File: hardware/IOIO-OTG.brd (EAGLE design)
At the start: 68.6 x 30.5 mm, 60 parts, among them Q1 IRLML2244, Q2 2N7002PW, Q3 MOSFET-NCHANNELAO3404A, U1 PIC24FJ256GB206, U2 TPS62133RGTT, U3 MIC5216

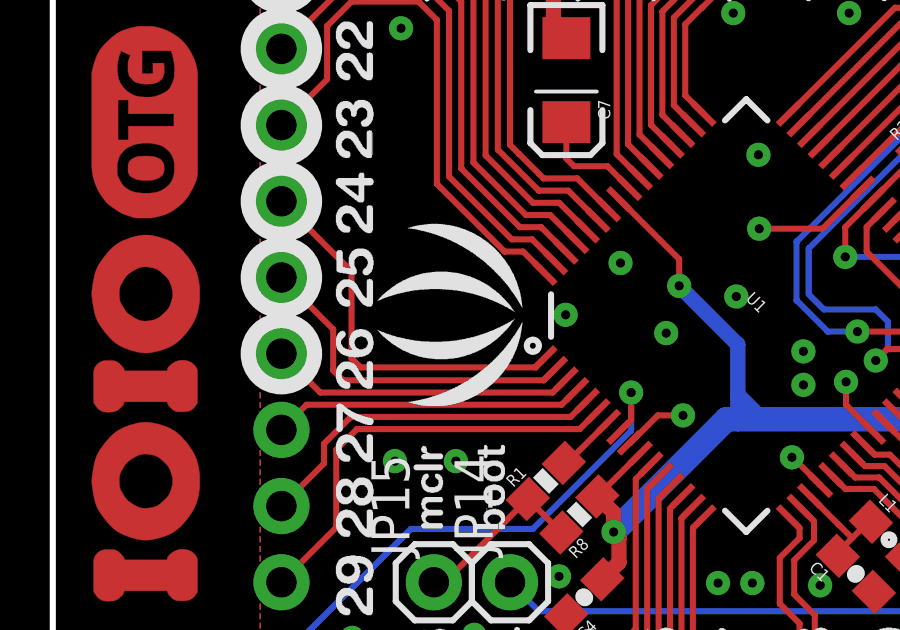
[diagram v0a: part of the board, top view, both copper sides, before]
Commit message: SparkFun Logo
Also, changed to v22a in schematic (it was still v22b from the copy
over)
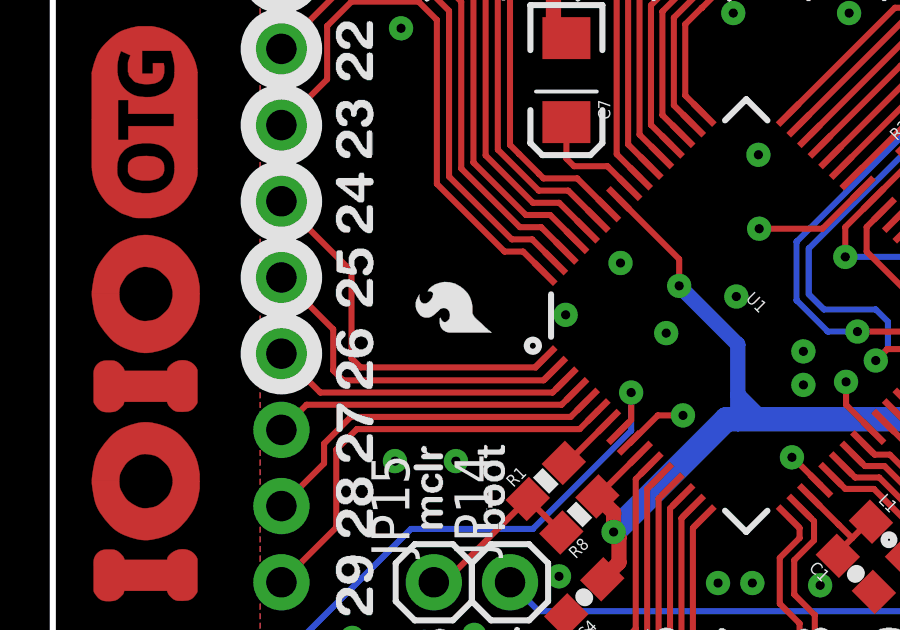
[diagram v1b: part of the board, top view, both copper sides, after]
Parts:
- removed U$13: (no value), Logo:LOGO_SILK
- removed U$15: (no value), Logo:SMALL_SEEED_LOGO
- added LOGO2: SFE_LOGO_NAME_FLAME.1_INCH, SparkFun-Aesthetics:SFE_LOGO_NAME_FLAME_.1
- added LOGO3: SFE_LOGO_FLAME.1_INCH, SparkFun-Aesthetics:SFE_LOGO_FLAME_.1
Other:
- board text removed: "www.seeedstudio.com"
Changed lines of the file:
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@@
 <layer number="27" name="tValues" color="7" fill="1" visible="no" active="yes"/>
 <layer number="28" name="bValues" color="7" fill="1" visible="no" active="yes"/>
-<layer number="29" name="tStop" color="7" fill="3" visible="yes" active="yes"/>
+<layer number="29" name="tStop" color="7" fill="3" visible="no" active="yes"/>
 <layer number="30" name="bStop" color="3" fill="6" visible="no" active="yes"/>
-<layer number="31" name="tCream" color="11" fill="4" visible="yes" active="yes"/>
+<layer number="31" name="tCream" color="11" fill="4" visible="no" active="yes"/>
 <layer number="32" name="bCream" color="3" fill="5" visible="no" active="yes"/>
 <layer number="33" name="tFinish" color="6" fill="3" visible="no" active="yes"/>
@@
 <layer number="47" name="Measures" color="7" fill="1" visible="no" active="yes"/>
 <layer number="48" name="Document" color="7" fill="1" visible="no" active="yes"/>
-<layer number="49" name="Reference" color="13" fill="1" visible="yes" active="yes"/>
+<layer number="49" name="Reference" color="13" fill="1" visible="no" active="yes"/>
 <layer number="50" name="dxf" color="7" fill="1" visible="no" active="yes"/>
 <layer number="51" name="tDocu" color="6" fill="1" visible="yes" active="yes"/>
@@
 <dimension x1="66.04" y1="2.54" x2="0" y2="2.54" x3="33.02" y3="35.56" textsize="1.016" layer="47" unit="inch"/>
 <dimension x1="68.58" y1="30.48" x2="0" y2="30.48" x3="34.29" y3="38.1" textsize="1.016" layer="47" unit="inch"/>
-<text x="5.334" y="26.416" size="1.4224" layer="22" ratio="18" rot="SMR270">www.seeedstudio.com</text>
 </plain>
 <attributes>
@@
 <attribute name="VALUE" x="65.554859375" y="20.8407" size="0.4064" layer="27" rot="R270"/>
 </element>
-<element name="U$13" library="Logo" package="LOGO_SILK" value="" x="13.97" y="15.24" rot="R90"/>
-<element name="U$15" library="Logo" package="SMALL_SEEED_LOGO" value="" x="1.905" y="15.875" rot="MR270"/>
+<element name="LOGO2" library="SparkFun-Aesthetics" package="SFE_LOGO_NAME_FLAME_.1" value="SFE_LOGO_NAME_FLAME.1_INCH" x="5.842" y="20.955" rot="MR270"/>
+<element name="LOGO3" library="SparkFun-Aesthetics" package="SFE_LOGO_FLAME_.1" value="SFE_LOGO_FLAME.1_INCH" x="14.986" y="14.351" rot="R90"/>
 </elements>
 <signals>
